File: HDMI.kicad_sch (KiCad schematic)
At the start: 27 parts, among them J1 HDMI_A, Q1 2N7002, Q2 2N7002, Q3 2N7002, U8 TPD4E05U06DQA, U9 TPD4E05U06DQA

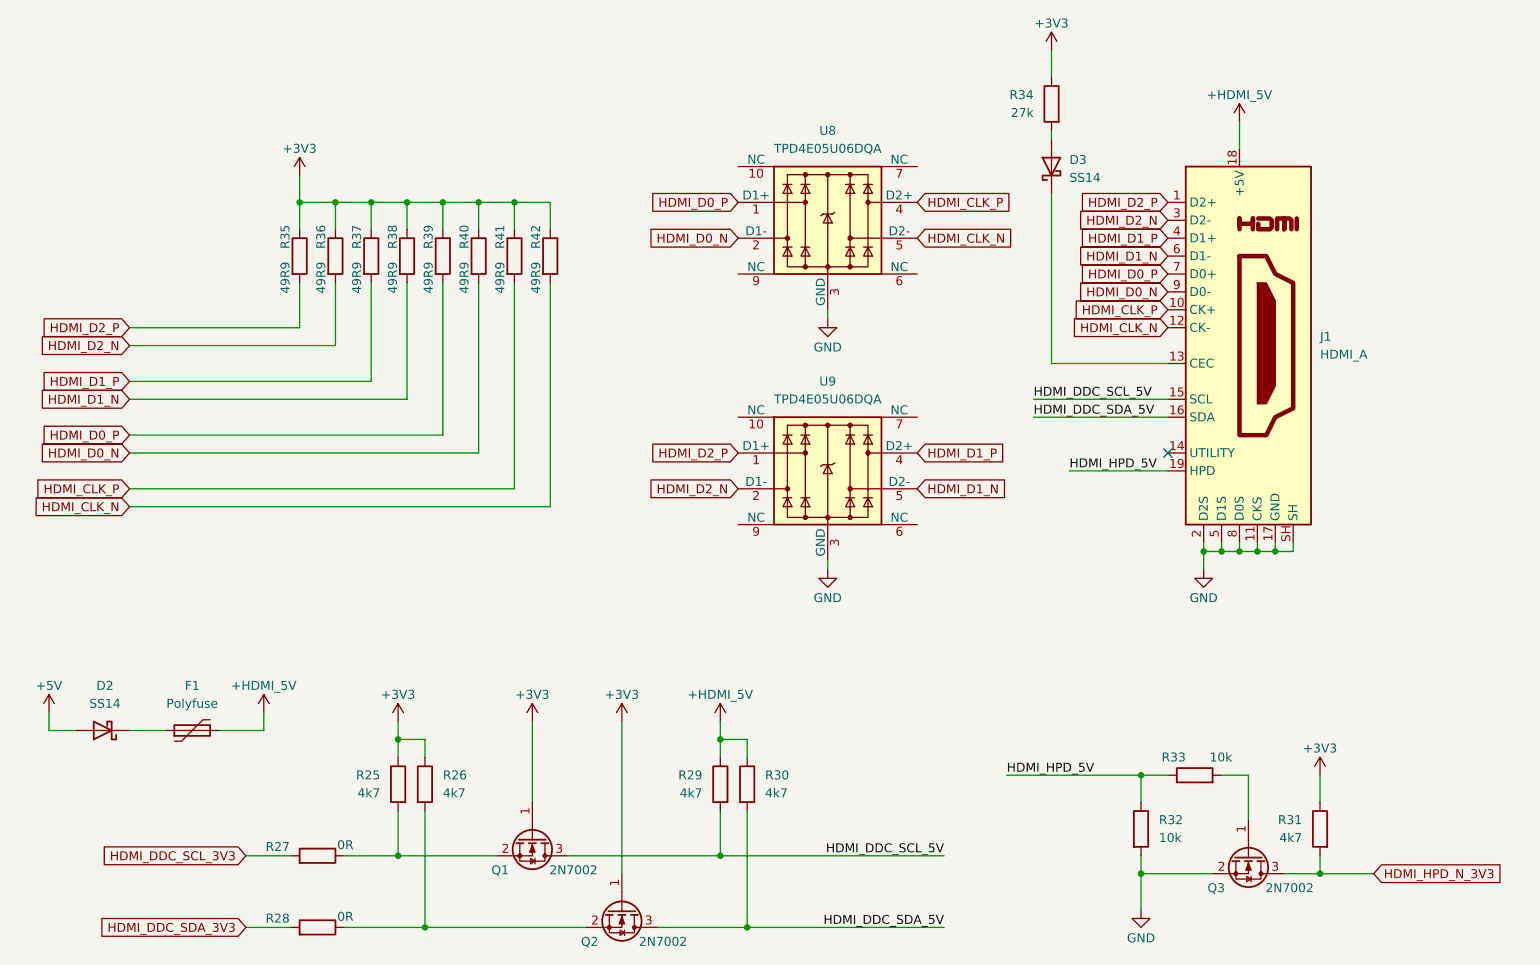
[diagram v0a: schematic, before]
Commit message: feat: finish ddr3 sch design
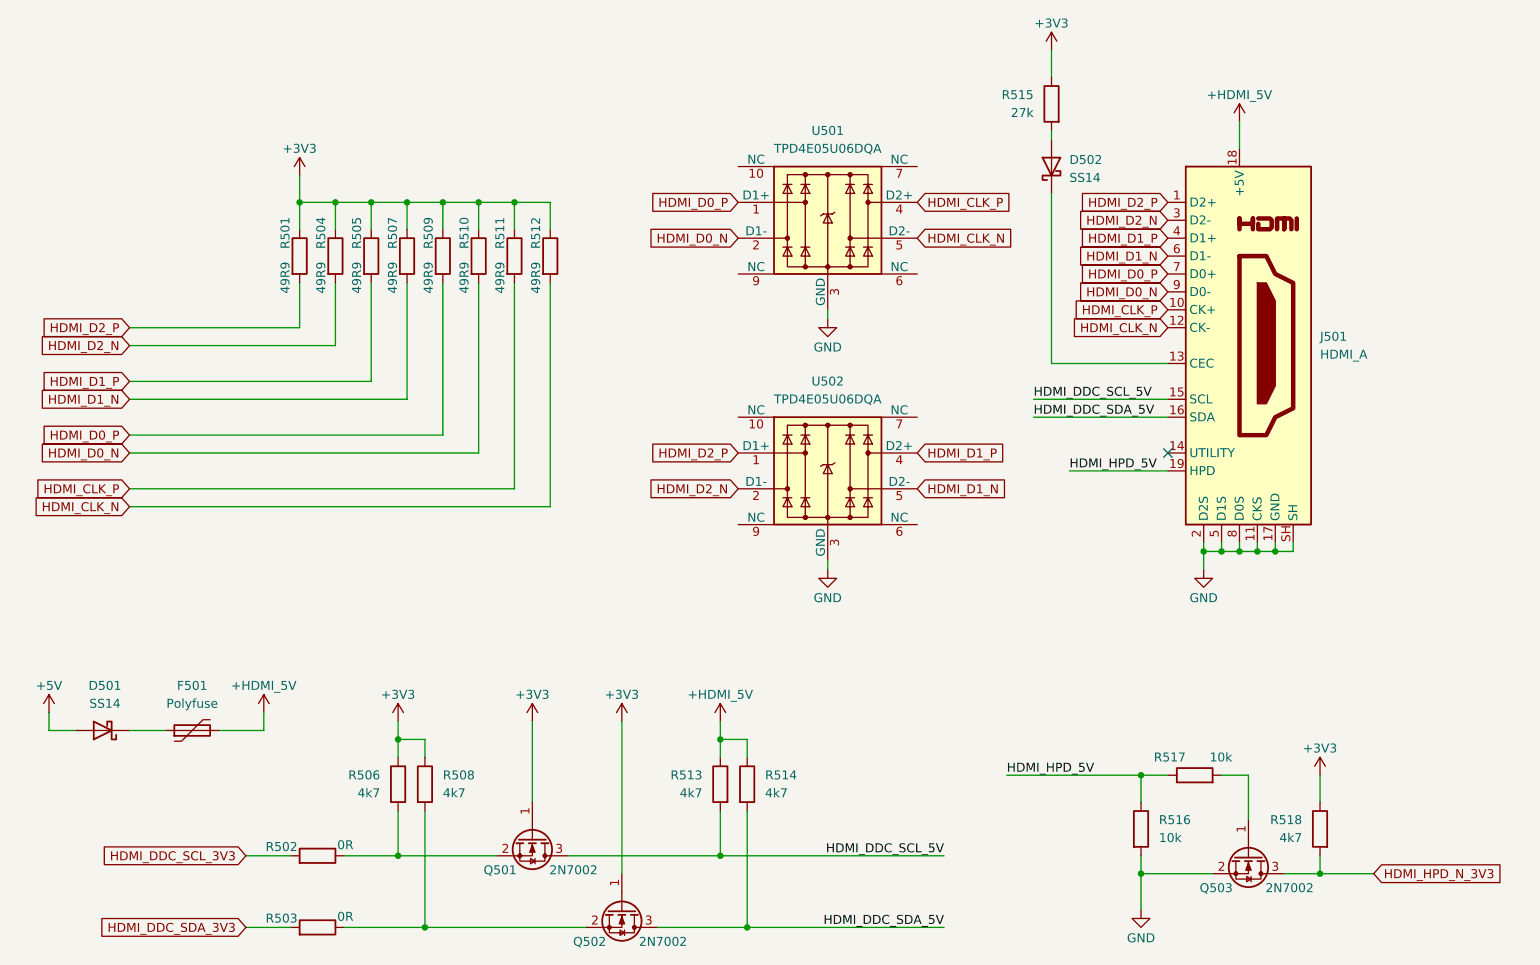
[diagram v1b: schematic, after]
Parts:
- renumbered D2 to D501, D3 to D502, F1 to F501, J1 to J501, Q1 to Q501, Q2 to Q502, Q3 to Q503, R35 to R501, R27 to R502, R28 to R503, R36 to R504, R37 to R505, R25 to R506, R38 to R507, R26 to R508, R39 to R509, R40 to R510, R41 to R511, R42 to R512, R29 to R513, R30 to R514, R34 to R515, R32 to R516, R33 to R517, R31 to R518, U8 to U501, U9 to U502

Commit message: feat: restart routing ddr
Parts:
- R516, R517: footprint (none) -> Resistor_SMD:R_0402_1005Metric
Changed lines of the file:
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@@
 			)
 		)
-		(property "Footprint" ""
+		(property "Footprint" "Resistor_SMD:R_0402_1005Metric"
 			(at 198.882 139.7 90)
 			(hide yes)
@@
 			)
 		)
-		(property "Footprint" ""
+		(property "Footprint" "Resistor_SMD:R_0402_1005Metric"
 			(at 208.28 133.858 90)
 			(hide yes)

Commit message: feat: continue routing
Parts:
- R506, R508, R513, R514, R518: footprint (none) -> Resistor_SMD:R_0402_1005Metric
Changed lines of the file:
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@@
 			)
 		)
-		(property "Footprint" ""
+		(property "Footprint" "Resistor_SMD:R_0402_1005Metric"
 			(at 97.282 133.35 90)
 			(hide yes)
@@
 			)
 		)
-		(property "Footprint" ""
+		(property "Footprint" "Resistor_SMD:R_0402_1005Metric"
 			(at 227.838 139.7 90)
 			(hide yes)
@@
 			)
 		)
-		(property "Footprint" ""
+		(property "Footprint" "Resistor_SMD:R_0402_1005Metric"
 			(at 97.028 133.35 90)
 			(hide yes)
@@
 			)
 		)
-		(property "Footprint" ""
+		(property "Footprint" "Resistor_SMD:R_0402_1005Metric"
 			(at 142.748 133.35 90)
 			(hide yes)
@@
 			)
 		)
-		(property "Footprint" ""
+		(property "Footprint" "Resistor_SMD:R_0402_1005Metric"
 			(at 143.002 133.35 90)
 			(hide yes)
